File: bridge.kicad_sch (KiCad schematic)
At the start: 13 parts, among them IC1 BD2320EFJ-LAE2, IC10 TC7W08FU_F_, IC13 Si8620BB-B-IS, IC4 BD14210G-LA, IC7 TC7S14F,LF, Q1 RD3L08BGNTL, Q4 RD3L08BGNTL

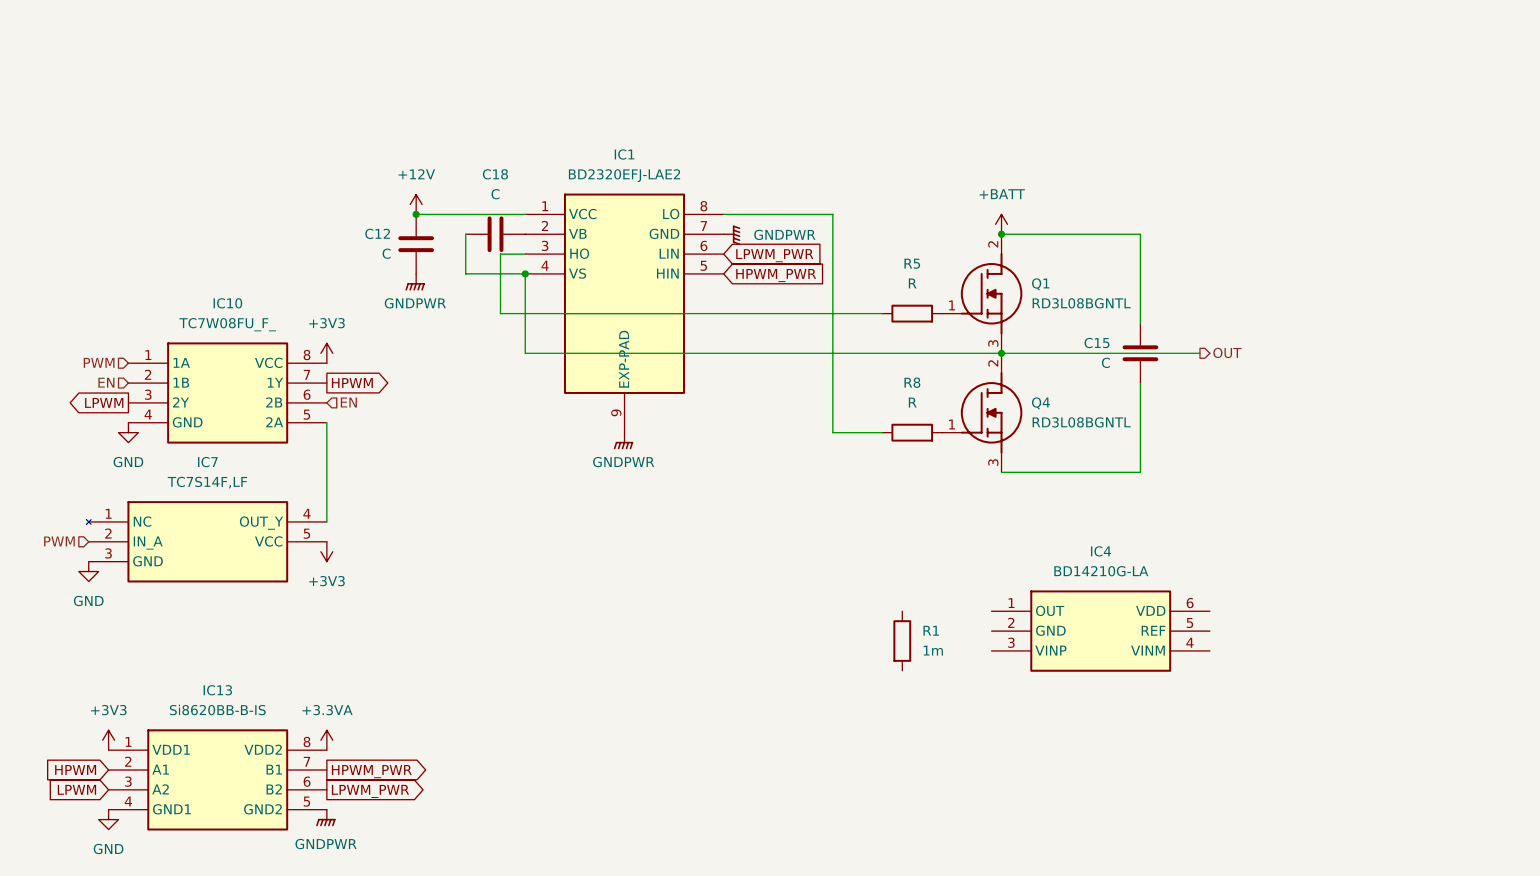
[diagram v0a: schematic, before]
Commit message: 回路図ほぼ完成 MOSFETのゲート抵抗の決め方よくわかんないです助けて
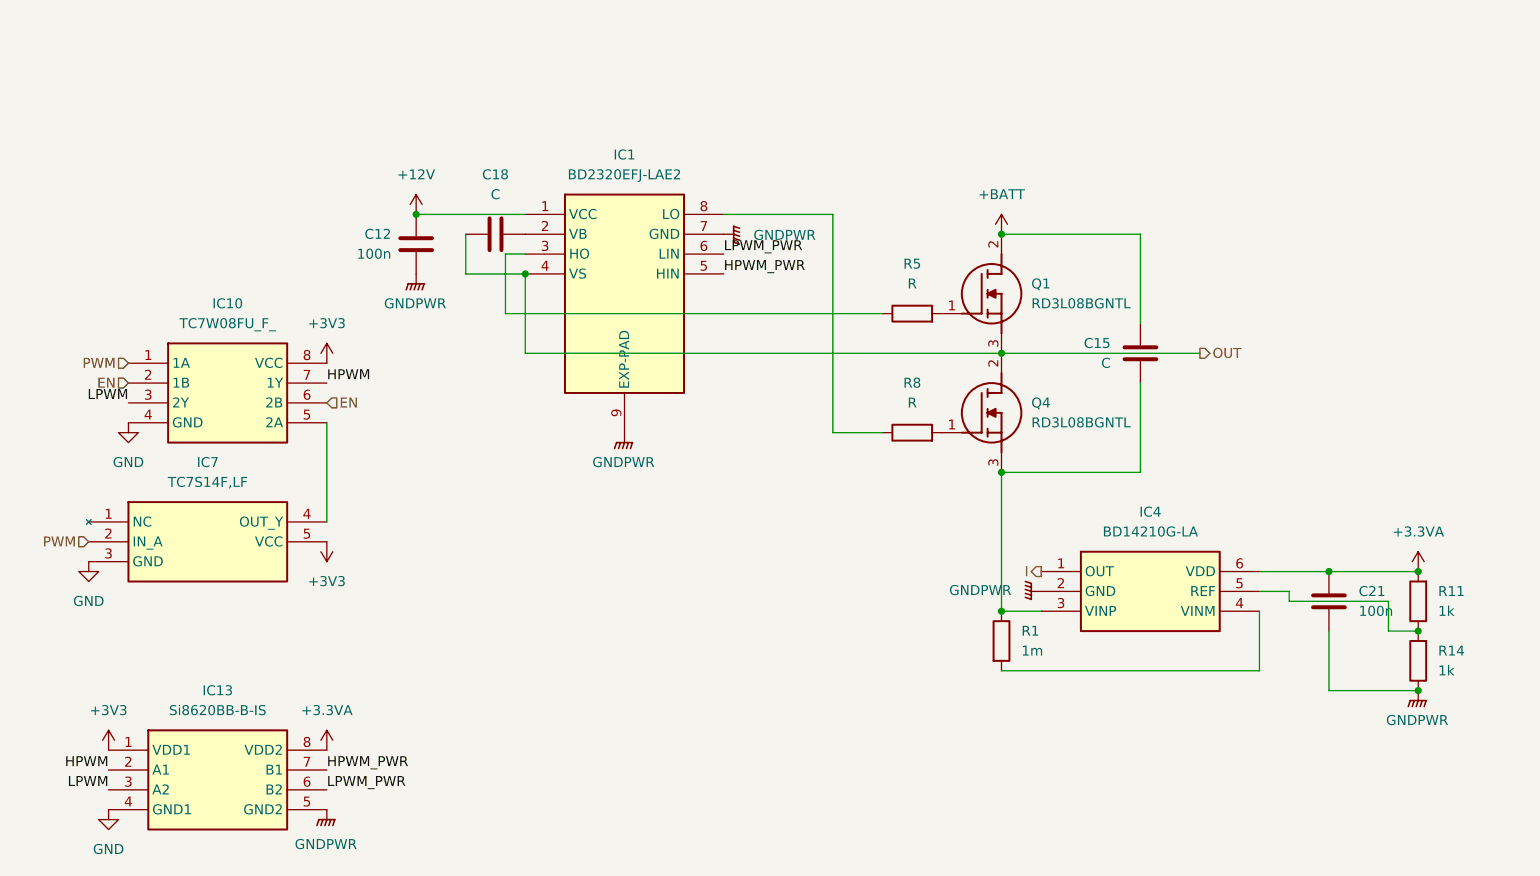
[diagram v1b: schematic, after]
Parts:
- added C21: 100n, symbol Device:C
- added R11, R14: 1k, symbol Device:R
- C12: value C -> 100n
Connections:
- net +3.3VA: now also IC4.6 (VDD), C21.1, R11.2
- net GNDPWR: now also IC4.2 (GND), C21.2, R14.1
- net at C15.2, Q4.3 (S): now also IC4.3 (VINP), R1.1
- net I: now reaches IC4.1 (OUT)
- net at IC4.4 (VINM): now also R1.2
- net at IC4.5 (REF): now also R11.1, R14.2
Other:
- moved on the sheet: IC4, R1

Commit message: 部品配置完了(暫定)
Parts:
- removed IC10: TC7W08FU_F_, SOP65P400X120-8N, symbol TC7W08FU_F_:TC7W08FU_F_
- removed R11, R14: 1k, symbol Device:R
- added U4, U7: 74AHC1G08, samacsys_lib:SOT95P275X140-5N, symbol 74xGxx:74AHC1G08
- C12, C15, C18, C21: footprint (none) -> Capacitor_SMD:C_0603_1608Metric_Pad1.08x0.95mm_HandSolder
- IC1: footprint SOIC127P600X100-9N -> samacsys_lib:SOIC127P600X100-9N
- IC13: footprint SOIC127P600X175-8N -> samacsys_lib:SOIC127P600X175-8N
- IC4: footprint SOP95P280X125-6N -> samacsys_lib:SOP95P280X125-6N
- IC7: footprint SOT95P275X140-5N -> samacsys_lib:SOT95P275X140-5N
- Q1, Q4: footprint RD3P175SNFRATL -> samacsys_lib:RD3P175SNFRATL
- R1, R5, R8: footprint (none) -> Resistor_SMD:R_0603_1608Metric_Pad0.98x0.95mm_HandSolder
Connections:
- net +3V3: now also U4.5 (VCC), U7.5 (VCC)
- net EN: now also U4.2, U7.1
- net GND: now also U4.3 (GND), U7.3 (GND)
- net GNDPWR: now also IC4.4 (VINM), R1.2
- net HPWM: now also U4.4
- net LPWM: now also U7.4
- net PWM: now also U4.1
- net OP_REF: now reaches IC4.5 (REF)
- net at IC7.4 (OUT_Y): now also U7.2
